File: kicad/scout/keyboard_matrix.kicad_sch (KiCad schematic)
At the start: 17 parts, among them SW10 SPST, SW11 SPST, SW12 SPST, SW13 SPST, SW14 SPST, SW15 SPST, SW16 SPST, SW17 SPST, SW18 SPST, SW2 SPST, SW3 SPST, SW4 SPST, SW5 SPST, SW6 SPST, SW7 SPST, SW8 SPST, SW9 SPST

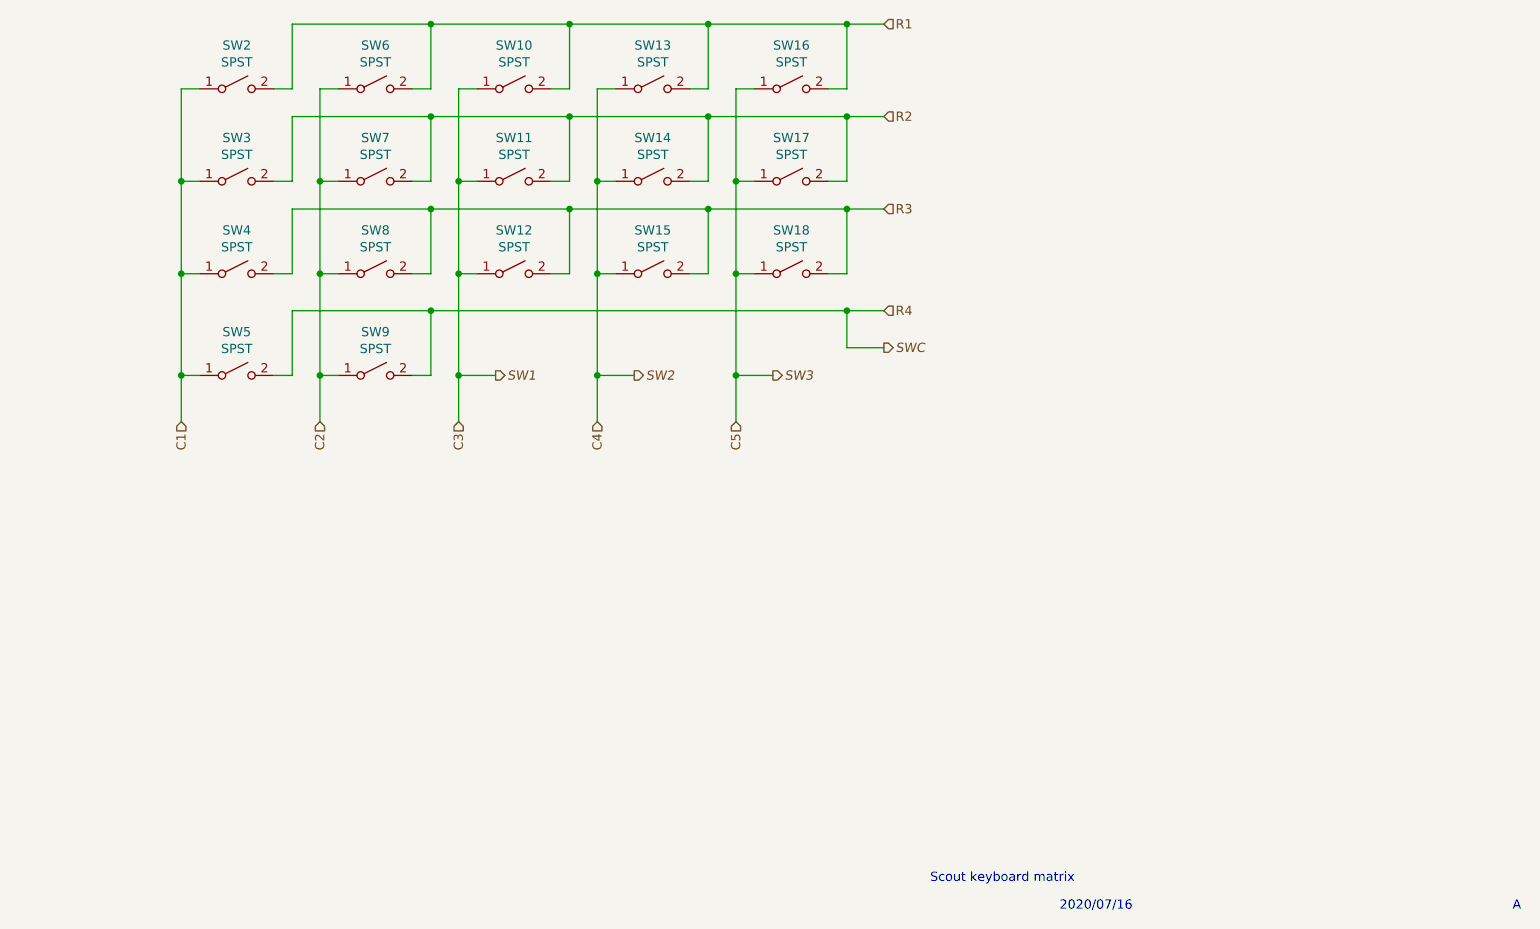
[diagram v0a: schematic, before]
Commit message: Add diodes
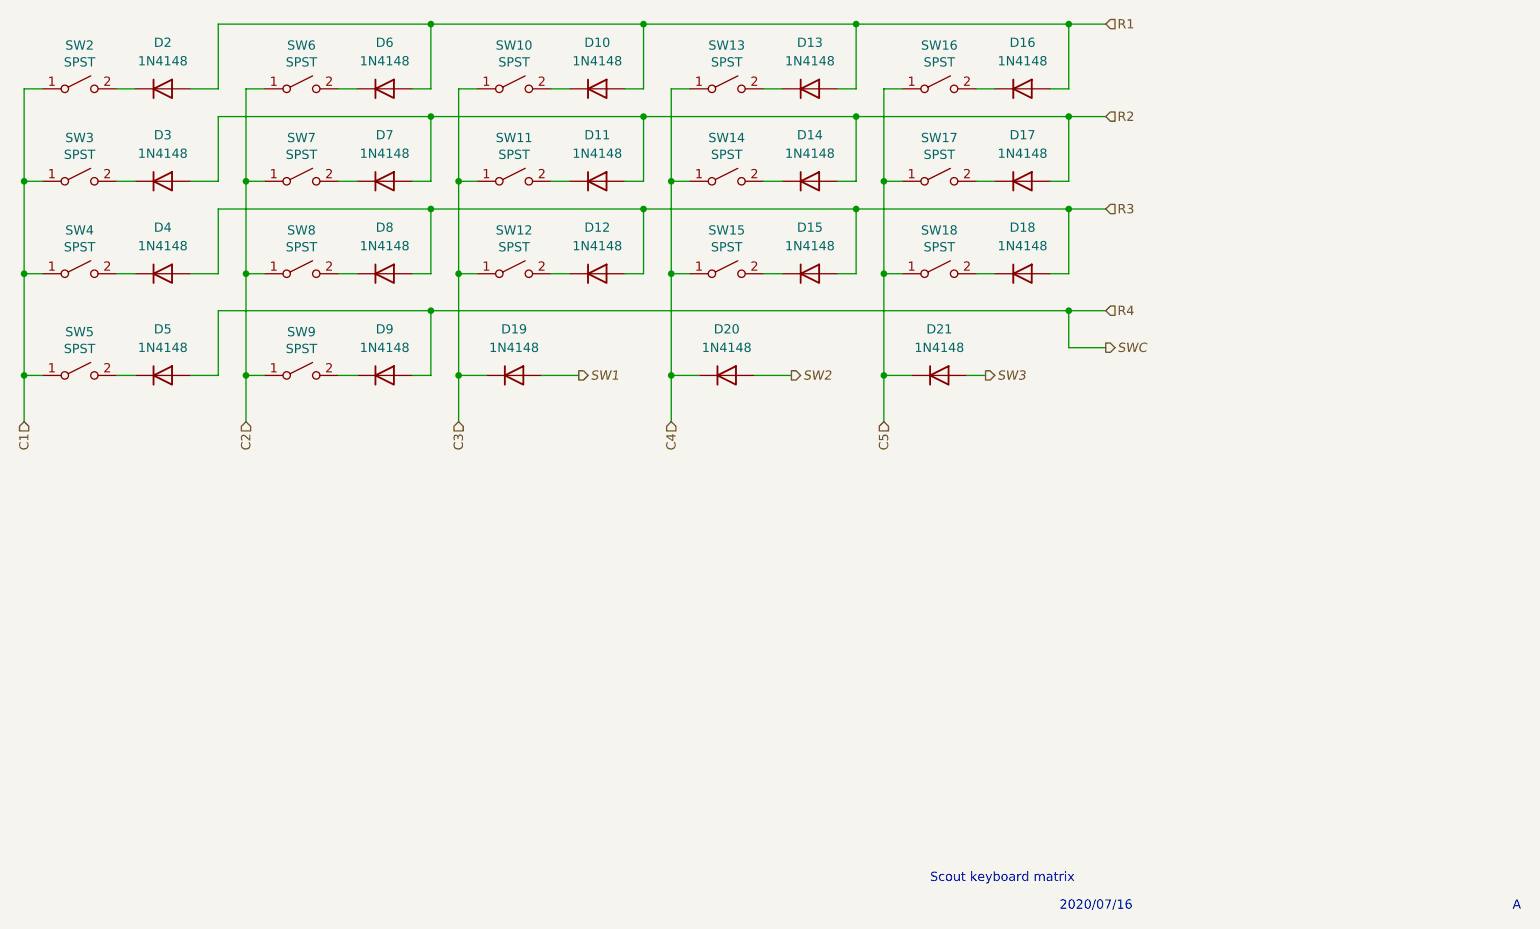
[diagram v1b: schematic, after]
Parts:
- added D10, D11, D12, D13, D14, D15, D16, D17, D18, D19, D2, D20, D21, D3, D4, D5, D6, D7, D8, D9: 1N4148, Diode_THT:D_DO-35_SOD27_P7.62mm_Horizontal, symbol Diode:1N4148
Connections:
- net C3: now also D19.1 (K)
- net C4: now also D20.1 (K)
- net C5: now also D21.1 (K)
- net R1: now also D10.2 (A), D13.2 (A), D16.2 (A), D2.2 (A), D6.2 (A); no longer SW10.2 (B), SW13.2 (B), SW16.2 (B), SW2.2 (B), SW6.2 (B)
- net R2: now also D11.2 (A), D14.2 (A), D17.2 (A), D3.2 (A), D7.2 (A); no longer SW11.2 (B), SW14.2 (B), SW17.2 (B), SW3.2 (B), SW7.2 (B)
- net R3: now also D12.2 (A), D15.2 (A), D18.2 (A), D4.2 (A), D8.2 (A); no longer SW12.2 (B), SW15.2 (B), SW18.2 (B), SW4.2 (B), SW8.2 (B)
- net R4: now also D5.2 (A), D9.2 (A); no longer SW5.2 (B), SW9.2 (B)
- new net: D2.1 (K), SW2.2 (B)
- new net: D6.1 (K), SW6.2 (B)
- new net: D10.1 (K), SW10.2 (B)
- new net: D13.1 (K), SW13.2 (B)
- new net: D16.1 (K), SW16.2 (B)
- new net: D3.1 (K), SW3.2 (B)
- new net: D7.1 (K), SW7.2 (B)
- new net: D11.1 (K), SW11.2 (B)
- new net: D14.1 (K), SW14.2 (B)
- new net: D17.1 (K), SW17.2 (B)
- new net: D4.1 (K), SW4.2 (B)
- new net: D8.1 (K), SW8.2 (B)
- new net: D12.1 (K), SW12.2 (B)
- new net: D15.1 (K), SW15.2 (B)
- new net: D18.1 (K), SW18.2 (B)
- new net: D5.1 (K), SW5.2 (B)
- new net: D9.1 (K), SW9.2 (B)
- new net SW1: D19.2 (A)
- new net SW2: D20.2 (A)
- new net SW3: D21.2 (A)
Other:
- moved on the sheet: SW13, SW14, SW15, SW16, SW17, SW18, SW2, SW3, SW4, SW5, SW6, SW7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
